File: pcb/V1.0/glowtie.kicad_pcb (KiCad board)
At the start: 2 copper layers, 127 x 57.1 mm, 39 parts, among them J1 USB_OTG, J10 POGO_3V3, J11 POGO_GND, J2 POGO_RX, J4 POGO_TX, J5 BOOT2, J6 GND_BATT1, J7 GND_BATT2, J8 VBATT1, J9 VBATT2, SW1 SW_SPDT, U1 MCP73831-2-OT, U2 MCP1826S-3302E, U3 ESP-12F

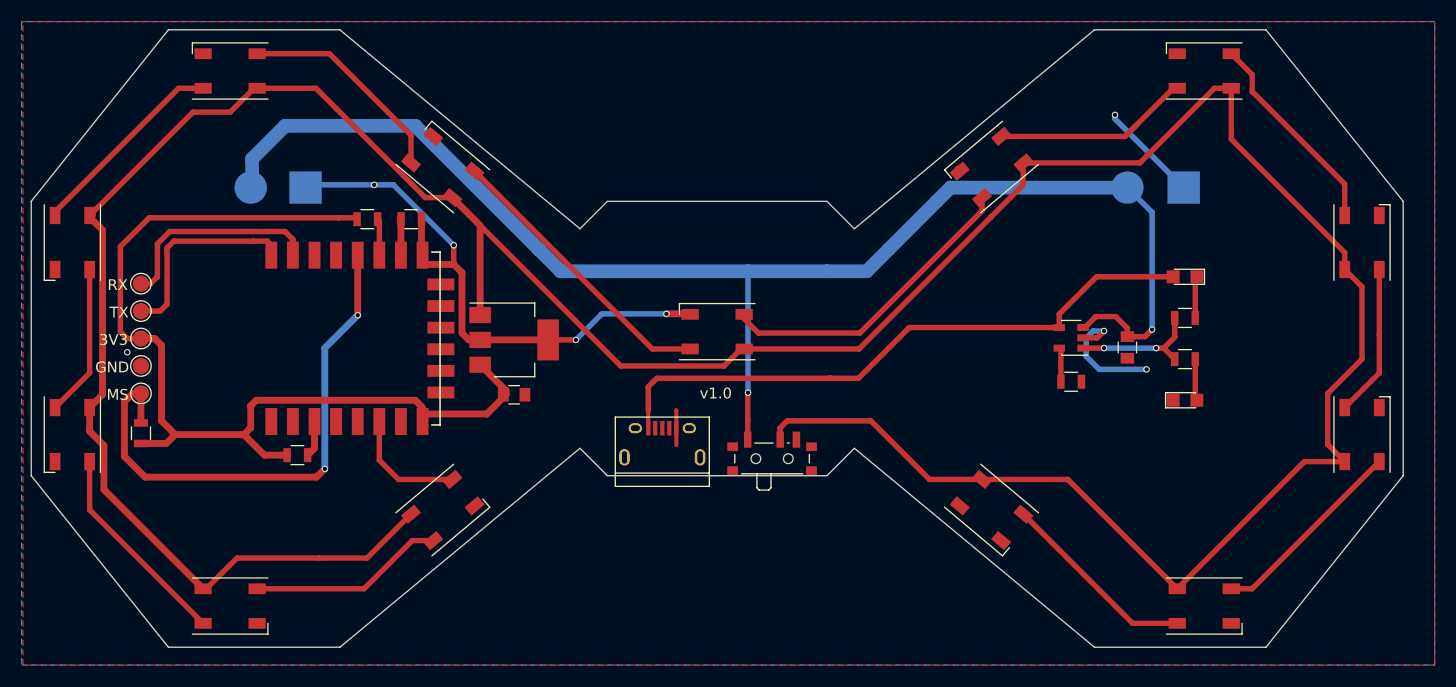
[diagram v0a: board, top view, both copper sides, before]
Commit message: updating pcb to v1.1 with better grounding, more widely used LDO pinout
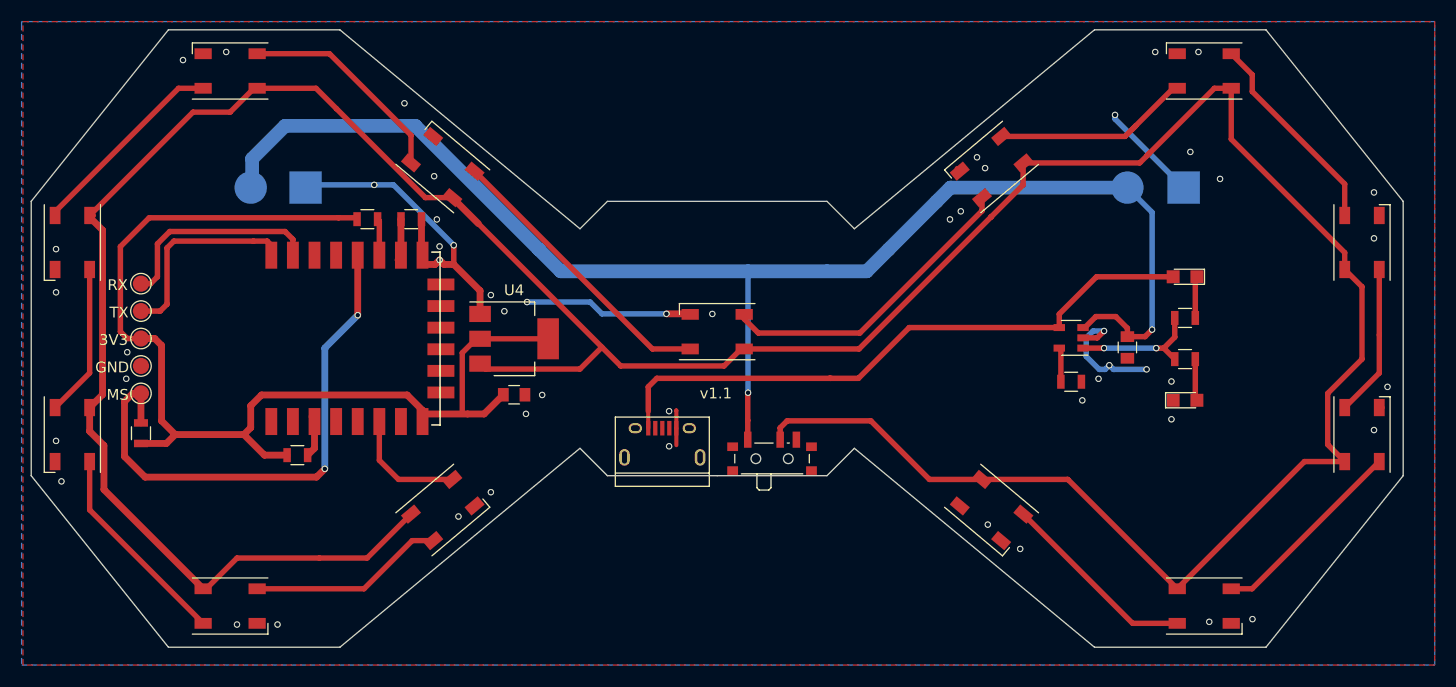
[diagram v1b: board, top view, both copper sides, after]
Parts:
- removed U2: MCP1826S-3302E, TO_SOT_Packages_SMD:SOT-223
- added U4: AZ1117-3.3, Package_TO_SOT_SMD:SOT-223-3_TabPin2, F.Cu at (57.4, 41.3)
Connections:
- J1 pad 2: Net-(J1-Pad2) -> unconnected-(J1-D--Pad2)
- J1 pad 3: Net-(J1-Pad3) -> unconnected-(J1-D+-Pad3)
- J1 pad 4: Net-(J1-Pad4) -> unconnected-(J1-ID-Pad4)
- J1 pad 6: Net-(J1-Pad6) -> unconnected-(J1-Shield-Pad6)
- LED13 pad 2: Net-(LED13-Pad2) -> unconnected-(LED13-DOUT-Pad2)
- SW1 pad 3: Net-(SW1-Pad3) -> unconnected-(SW1-C-Pad3)
- U3 pad 1: Net-(U3-Pad1) -> unconnected-(U3-REST-Pad1)
- U3 pad 13: Net-(U3-Pad13) -> unconnected-(U3-GPIO4-Pad13)
- U3 pad 14: Net-(U3-Pad14) -> unconnected-(U3-GPIO5-Pad14)
- U3 pad 17: Net-(U3-Pad17) -> unconnected-(U3-CS0-Pad17)
- U3 pad 18: Net-(U3-Pad18) -> unconnected-(U3-MISO-Pad18)
- U3 pad 19: Net-(U3-Pad19) -> unconnected-(U3-GPIO9-Pad19)
- U3 pad 2: Net-(U3-Pad2) -> unconnected-(U3-ADC-Pad2)
- U3 pad 20: Net-(U3-Pad20) -> unconnected-(U3-GPIO10-Pad20)
- U3 pad 21: Net-(U3-Pad21) -> unconnected-(U3-MOSI-Pad21)
- U3 pad 22: Net-(U3-Pad22) -> unconnected-(U3-SCLK-Pad22)
- U3 pad 4: Net-(U3-Pad4) -> unconnected-(U3-GPIO16-Pad4)
- U3 pad 5: Net-(U3-Pad5) -> unconnected-(U3-GPIO14-Pad5)
- U3 pad 7: Net-(U3-Pad7) -> unconnected-(U3-GPIO13-Pad7)
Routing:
- net +3V3: track 90.9 -> 101.8 mm
- net GND: track 80.7 -> 73.4 mm, vias 8 -> 52
- net +BATT: track 312.6 -> 316.6 mm
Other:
- net class Default removed
- net class sadfs removed
- net class test removed
- board text added: "v1.1"
- board text removed: "v1.0"

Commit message: adds v1.1 and docs page
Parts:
- added REF**: Fiducial_1mm_Mask2mm, Fiducial:Fiducial_1mm_Mask2mm, F.Cu at (14.8, 41.2)
- added REF**: Fiducial_1mm_Mask2mm, Fiducial:Fiducial_1mm_Mask2mm, F.Cu at (127.2, 65.2)
- added REF**: Fiducial_1mm_Mask2mm, Fiducial:Fiducial_1mm_Mask2mm, F.Cu at (112.2, 15.2)
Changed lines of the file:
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@@
       (drillshape 0)
       (scaleselection 1)
-      (outputdirectory "gerbers/v1.0/fab/")
+      (outputdirectory "../v1.1/out/")
     )
   )
@@
       (stroke (width 0.01) (type solid)) (fill solid) (layer "F.Mask"))
   )
+  (footprint "Fiducial:Fiducial_1mm_Mask2mm" (layer "F.Cu")
+    (at 14.75 41.25)
+    (descr "Circular Fiducial, 1mm bare copper, 2mm soldermask opening (Level A)")
+    (tags "fiducial")
+    (attr smd)
+    (fp_text reference "REF**" (at 0 -2) (layer "F.SilkS") hide
+        (effects (font (size 1 1) (thickness 0.15)))
+    )
+    (fp_text value "Fiducial_1mm_Mask2mm" (at 0 2) (layer "F.Fab")
+        (effects (font (size 1 1) (thickness 0.15)))
+    )
+    (fp_text user "${REFERENCE}" (at 0 0) (layer "F.Fab")
+        (effects (font (size 0.4 0.4) (thickness 0.06)))
+    )
+    (fp_circle (center 0 0) (end 1.25 0)
+      (stroke (width 0.05) (type solid)) (fill none) (layer "F.CrtYd"))
+    (fp_circle (center 0 0) (end 1 0)
+      (stroke (width 0.1) (type solid)) (fill none) (layer "F.Fab"))
+    (pad "" smd circle (at 0 0) (size 1 1) (layers "F.Cu" "F.Mask")
+      (solder_mask_margin 0.5) (clearance 0.5))
+  )
   (footprint "Package_TO_SOT_SMD:SOT-223-3_TabPin2" (layer "F.Cu")
     (at 57.4 41.3)
@@
     (property "ki_keywords" "Fixed Voltage Regulator 1A Positive LDO")
     (attr smd)
-    (fp_text reference "U4" (at 0 -4.5) (layer "F.SilkS")
+    (fp_text reference "U4" (at 0 -4.5) (layer "F.SilkS") hide
         (effects (font (size 1 1) (thickness 0.15)))
     )
@@
       (rotate (xyz 0 0 0))
     )
+  )
+  (footprint "Fiducial:Fiducial_1mm_Mask2mm" (layer "F.Cu")
+    (at 127.25 65.25)
+    (descr "Circular Fiducial, 1mm bare copper, 2mm soldermask opening (Level A)")
+    (tags "fiducial")
+    (attr smd)
+    (fp_text reference "REF**" (at 0 -2) (layer "F.SilkS") hide
+        (effects (font (size 1 1) (thickness 0.15)))
+    )
+    (fp_text value "Fiducial_1mm_Mask2mm" (at 0 2) (layer "F.Fab")
+        (effects (font (size 1 1) (thickness 0.15)))
+    )
+    (fp_text user "${REFERENCE}" (at 0 0) (layer "F.Fab")
+        (effects (font (size 0.4 0.4) (thickness 0.06)))
+    )
+    (fp_circle (center 0 0) (end 1.25 0)
+      (stroke (width 0.05) (type solid)) (fill none) (layer "F.CrtYd"))
+    (fp_circle (center 0 0) (end 1 0)
+      (stroke (width 0.1) (type solid)) (fill none) (layer "F.Fab"))
+    (pad "" smd circle (at 0 0) (size 1 1) (layers "F.Cu" "F.Mask")
+      (solder_mask_margin 0.5) (clearance 0.5))
+  )
+  (footprint "Fiducial:Fiducial_1mm_Mask2mm" (layer "F.Cu")
+    (at 112.25 15.25)
+    (descr "Circular Fiducial, 1mm bare copper, 2mm soldermask opening (Level A)")
+    (tags "fiducial")
+    (attr smd)
+    (fp_text reference "REF**" (at 0 -2) (layer "F.SilkS") hide
+        (effects (font (size 1 1) (thickness 0.15)))
+    )
+    (fp_text value "Fiducial_1mm_Mask2mm" (at 0 2) (layer "F.Fab")
+        (effects (font (size 1 1) (thickness 0.15)))
+    )
+    (fp_text user "${REFERENCE}" (at 0 0) (layer "F.Fab")
+        (effects (font (size 0.4 0.4) (thickness 0.06)))
+    )
+    (fp_circle (center 0 0) (end 1.25 0)
+      (stroke (width 0.05) (type solid)) (fill none) (layer "F.CrtYd"))
+    (fp_circle (center 0 0) (end 1 0)
+      (stroke (width 0.1) (type solid)) (fill none) (layer "F.Fab"))
+    (pad "" smd circle (at 0 0) (size 1 1) (layers "F.Cu" "F.Mask")
+      (solder_mask_margin 0.5) (clearance 0.5))
   )
   (gr_line (start 63.5 31.115) (end 66.04 28.575)
@@
   (segment (start 44.925 52.545) (end 44.925 48.26) (width 0.5) (layer "F.Cu") (net 25))
   (segment (start 51.686651 54.31736) (end 46.69736 54.31736) (width 0.5) (layer "F.Cu") (net 25))
-  (segment (start 125.715 64.44) (end 137.49 52.665) (width 0.5) (layer "F.Cu") (net 26))
-  (segment (start 123.785 64.44) (end 125.715 64.44) (width 0.5) (layer "F.Cu") (net 26))
+  (segment (start 126.225 62) (end 128.155 62) (width 0.5) (layer "F.Cu") (net 26))
+  (segment (start 123.785 64.44) (end 126.225 62) (width 0.5) (layer "F.Cu") (net 26))
+  (segment (start 128.155 62) (end 137.49 52.665) (width 0.5) (layer "F.Cu") (net 26))
   (segment (start 114.652273 67.64) (end 104.543571 57.531298) (width 0.5) (layer "F.Cu") (net 27))
   (segment (start 118.785 67.64) (end 114.652273 67.64) (width 0.5) (layer "F.Cu") (net 27))
